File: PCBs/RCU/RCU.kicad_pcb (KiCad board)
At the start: 4 copper layers, 99 x 139 mm, 148 parts, among them J100 Conn_01x02, J200 USB_C_Receptacle_USB2.0, J201 Conn_01x05, J300 Right_Motor_Screw_Terminal, J301 Right_Encoder_Conn, J302 Left_Motor_Screw_Terminal, J303 Left_Encoder_Conn, J400 USB_C_Receptacle_USB2.0, Q400 2N7002NXAKR (NMOS), Q401 2N7002NXAKR (NMOS), Q402 BSS84AK,215 (PMOS), Q403 2N7002NXAKR (NMOS), SW201 SW_Push, SW400 SW_Push, SW401 SW_SPDT, U100 LM2576S-ADJ, U101 AP63203WU, U102 AZ1117-3.3, U200 STM32G0B1CBT6, U201 USBLC6-2SC6, U300 OPA320, U301 DRV8876, U302 OPA320, U303 DRV8876, U400 USBLC6-2SC6, U401 CH340C, U402 ESP32-MINI-1, U403 DG2788ADN-T1-GE4, U500 APDS-9306-065, U501 LSM6DS3, U502 SHT30-DIS, U600 ADC121C027CIMK/NOPB, U601 OPA320, U602 ADC121C027CIMK/NOPB, U603 OPA320, U700 SST26VF032BT-104I/SM, Y200 16MHz

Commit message: Course layout complete, added all 3d models
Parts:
- moved D104 35.0 mm to (128.5, 28.1)
- moved D103 23.2 mm to (130.1, 32.7), turned to -90 degrees
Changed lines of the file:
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@@
     (pad "2" smd rect (at 1.59 0 270) (size 1.18 1.17) (layers "F.Cu" "F.Paste" "F.Mask")
       (net 8 "+5C") (pinfunction "A") (pintype "passive") (solder_mask_margin 0.102))
+    (model "${KICAD6_3DMODEL_DIR}/Diode_SMD.3dshapes/D_SOD-123F.step"
+      (offset (xyz 0 0 0))
+      (scale (xyz 1 1 1))
+      (rotate (xyz 0 0 0))
+    )
   )
   (footprint "Resistor_SMD:R_0603_1608Metric" (layer "F.Cu")
@@
     (pad "2" smd rect (at 1.59 0) (size 1.18 1.17) (layers "F.Cu" "F.Paste" "F.Mask")
       (net 1 "+BATT") (pinfunction "A") (pintype "passive") (solder_mask_margin 0.102))
+    (model "${KICAD6_3DMODEL_DIR}/Diode_SMD.3dshapes/D_SOD-123F.step"
+      (offset (xyz 0 0 0))
+      (scale (xyz 1 1 1))
+      (rotate (xyz 0 0 0))
+    )
   )
   (footprint "Resistor_SMD:R_0603_1608Metric" (layer "F.Cu")
@@
   )
   (footprint "Schottky_Diode:SODFL3719X135N" (layer "F.Cu")
-    (at 152.5 26.7)
+    (at 130.1 32.7 -90)
     (property "Sheetfile" "Power.kicad_sch")
     (property "Sheetname" "[1] Power")
     (attr smd)
-    (fp_text reference "D103" (at 0.07 -2.2) (layer "F.SilkS")
+    (fp_text reference "D103" (at 0.07 -2.2 90) (layer "F.SilkS")
       (effects (font (size 0.787402 0.787402) (thickness 0.15)))
     )
-    (fp_text value "SM5817" (at 4.57 2.2) (layer "F.Fab")
+    (fp_text value "SM5817" (at 4.57 2.2 90) (layer "F.Fab")
       (effects (font (size 0.787402 0.787402) (thickness 0.15)))
     )
@@
     (fp_line (start -1.425 -0.95) (end -1.425 0.95) (layer "F.Fab") (width 0.127))
     (fp_circle (center -3.18 0) (end -3.08 0) (layer "F.Fab") (width 0.2) (fill none))
-    (pad "1" smd rect (at -1.59 0) (size 1.18 1.17) (layers "F.Cu" "F.Paste" "F.Mask")
+    (pad "1" smd rect (at -1.59 0 270) (size 1.18 1.17) (layers "F.Cu" "F.Paste" "F.Mask")
       (net 29 "Net-(D103-Pad1)") (pinfunction "K") (pintype "passive") (solder_mask_margin 0.102))
-    (pad "2" smd rect (at 1.59 0) (size 1.18 1.17) (layers "F.Cu" "F.Paste" "F.Mask")
+    (pad "2" smd rect (at 1.59 0 270) (size 1.18 1.17) (layers "F.Cu" "F.Paste" "F.Mask")
       (net 12 "+5F") (pinfunction "A") (pintype "passive") (solder_mask_margin 0.102))
+    (model "${KICAD6_3DMODEL_DIR}/Diode_SMD.3dshapes/D_SOD-123F.step"
+      (offset (xyz 0 0 0))
+      (scale (xyz 1 1 1))
+      (rotate (xyz 0 0 0))
+    )
   )
   (footprint "Capacitor_SMD:C_0603_1608Metric" (layer "F.Cu")
@@
   )
   (footprint "Schottky_Diode:SODFL3719X135N" (layer "F.Cu")
-    (at 163.5 26.7)
+    (at 128.5 28.1)
     (property "Sheetfile" "Power.kicad_sch")
     (property "Sheetname" "[1] Power")
@@
     (pad "2" smd rect (at 1.59 0) (size 1.18 1.17) (layers "F.Cu" "F.Paste" "F.Mask")
       (net 29 "Net-(D103-Pad1)") (pinfunction "A") (pintype "passive") (solder_mask_margin 0.102))
+    (model "${KICAD6_3DMODEL_DIR}/Diode_SMD.3dshapes/D_SOD-123F.step"
+      (offset (xyz 0 0 0))
+      (scale (xyz 1 1 1))
+      (rotate (xyz 0 0 0))
+    )
   )
   (footprint "Resistor_SMD:R_0603_1608Metric" (layer "F.Cu")

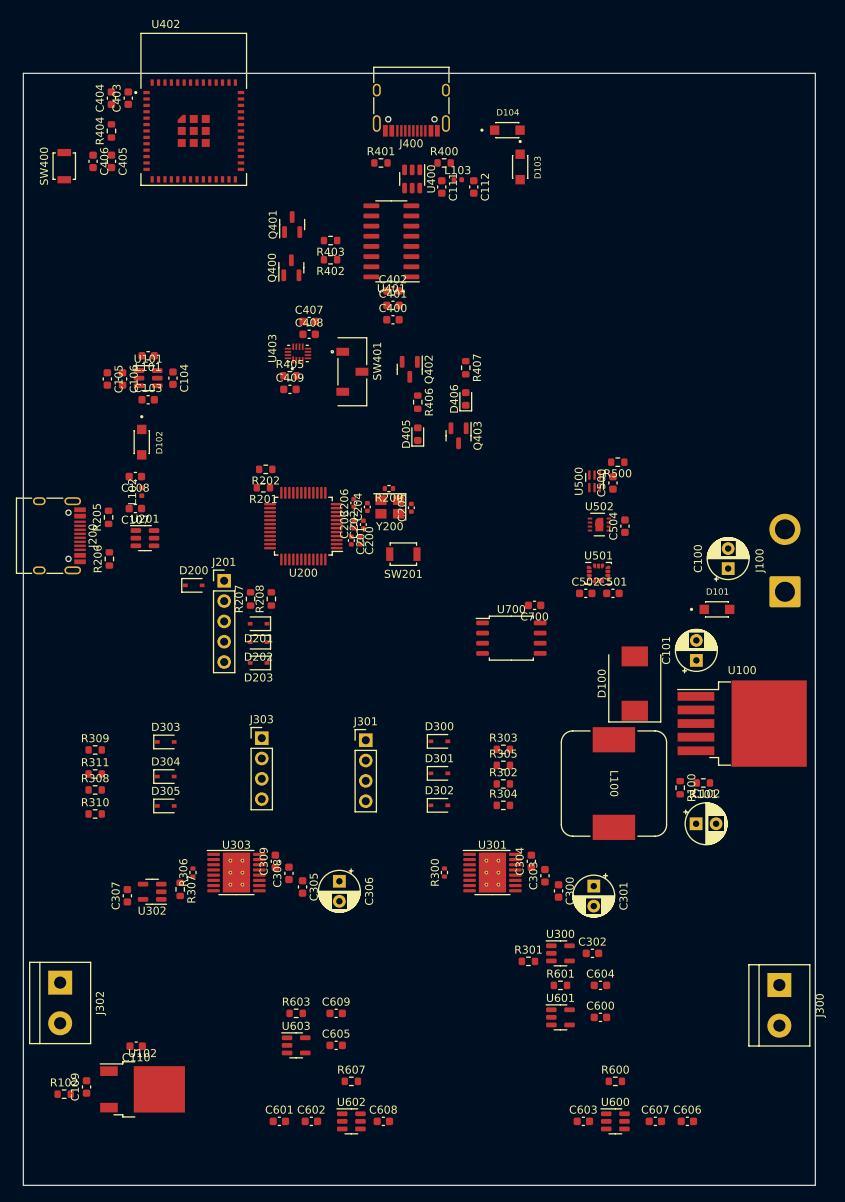
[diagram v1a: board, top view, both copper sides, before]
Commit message: Added drill/place file and grid origin
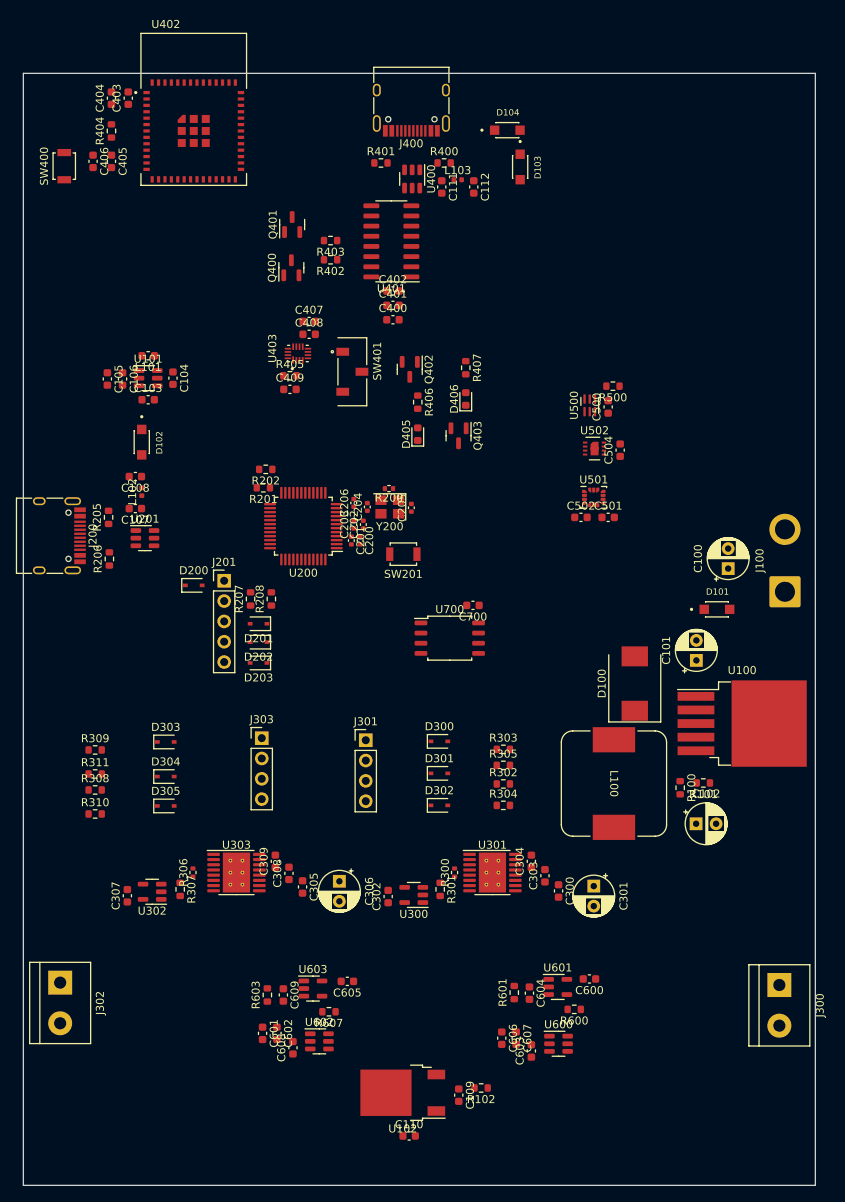
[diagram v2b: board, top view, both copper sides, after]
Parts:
- moved R102 52.1 mm to (125.2, 147.8), turned to 180 degrees
- moved C109 46.5 mm to (122.4, 148.7), turned to -90 degrees
- moved C110 35.9 mm to (116.2, 153.8), turned to 0 degrees
- moved U102 32.5 mm to (115.4, 148.4), turned to 180 degrees
- moved C302 26.5 mm to (113.6, 123.9), turned to 90 degrees
- moved C606 25.4 mm to (127.8, 141.6), turned to -90 degrees
- moved C607 20.3 mm to (129.6, 141.6), turned to -90 degrees
- moved U300 19.7 mm to (116.8, 123.7), turned to 180 degrees
- moved C608 14.6 mm to (101.7, 142.8), turned to 90 degrees
- moved R301 14.2 mm to (120.1, 123.0), turned to -90 degrees
- moved U600 12.0 mm to (134.9, 142.3)
- moved C602 11.8 mm to (99.7, 141.0), turned to -90 degrees
- moved C601 11.2 mm to (97.9, 141.0), turned to -90 degrees
- moved C603 10.9 mm to (131.5, 143.2), turned to 90 degrees
- moved U602 10.8 mm to (105.0, 142.0)
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
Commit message: More rearangment, added 3d model to light and temp/humidity sensor
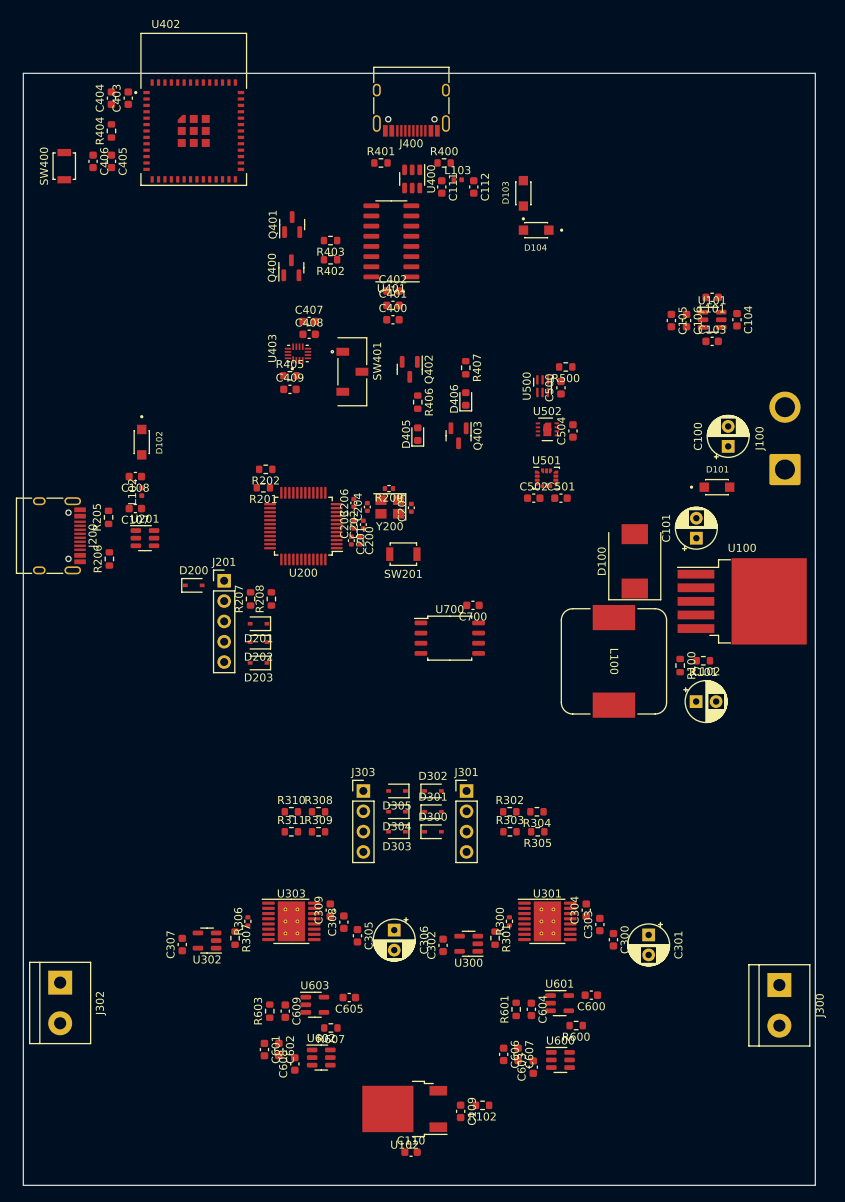
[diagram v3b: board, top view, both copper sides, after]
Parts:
- moved C103 70.9 mm to (154.1, 54.5)
- moved C104 70.9 mm to (157.2, 51.8)
- moved C105 70.9 mm to (149.0, 51.9)
- moved C106 70.9 mm to (150.9, 51.9)
- moved L101 70.9 mm to (154.1, 49.0)
- moved U101 70.9 mm to (154.1, 51.8)
- moved D303 31.0 mm to (114.7, 115.8), turned to 180 degrees
- moved R309 29.7 mm to (104.9, 115.8)
- moved D304 29.2 mm to (114.7, 113.3), turned to 180 degrees
- moved D305 29.0 mm to (114.7, 110.7), turned to 180 degrees
- moved R308 28.1 mm to (104.9, 113.3)
- moved R311 25.6 mm to (101.5, 115.8)
- moved R310 24.5 mm to (101.5, 113.3)
- moved C100 15.3 mm to (156.1, 67.6)
- moved D100 15.3 mm to (144.4, 82.0)
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
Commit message: Performed ground pour on internal ground layer
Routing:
- net +3V3: track 0.00 -> 6.09 mm
- added copper zone on F.Cu, net GND
- added copper zone on In1.Cu, net GND
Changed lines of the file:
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@@
   (gr_line (start 68 160) (end 68 21) (layer "Edge.Cuts") (width 0.1))
   (gr_line (start 167 160) (end 68 160) (layer "Edge.Cuts") (width 0.1))
+  (segment (start 108.43 78.35) (end 109 78.92) (width 0.3) (layer "F.Cu") (net 6))
+  (segment (start 109 78.92) (end 108.93 78.85) (width 0.3) (layer "F.Cu") (net 6))
+  (segment (start 109.27 77.85) (end 109.3 77.88) (width 0.3) (layer "F.Cu") (net 6))
+  (segment (start 107.1625 77.85) (end 109.27 77.85) (width 0.3) (layer "F.Cu") (net 6))
+  (segment (start 108.93 78.85) (end 107.1625 78.85) (width 0.3) (layer "F.Cu") (net 6))
+  (segment (start 107.1625 78.35) (end 108.43 78.35) (width 0.3) (layer "F.Cu") (net 6))
+  (zone (net 2) (net_name "GND") (layer "F.Cu") (hatch edge 0.508)
+    (connect_pads yes (clearance 0.15))
+    (min_thickness 0.254) (filled_areas_thickness no)
+    (fill yes (thermal_gap 0.508) (thermal_bridge_width 0.508))
+    (polygon
+      (pts
+        (xy 110.6 80.4)
+        (xy 108.5 80.4)
+        (xy 108.5 79.5)
+        (xy 110.6 79.5)
+      )
+    )
+  )
+  (zone (net 2) (net_name "GND") (layer "In1.Cu") (hatch edge 0.508)
+    (connect_pads (clearance 0.4))
+    (min_thickness 0.3) (filled_areas_thickness no)
+    (fill yes (thermal_gap 0.508) (thermal_bridge_width 0.508))
+    (polygon
+      (pts
+        (xy 167 160)
+        (xy 68 160)
+        (xy 68 21)
+        (xy 167 21)
+      )
+    )
+  )
 )

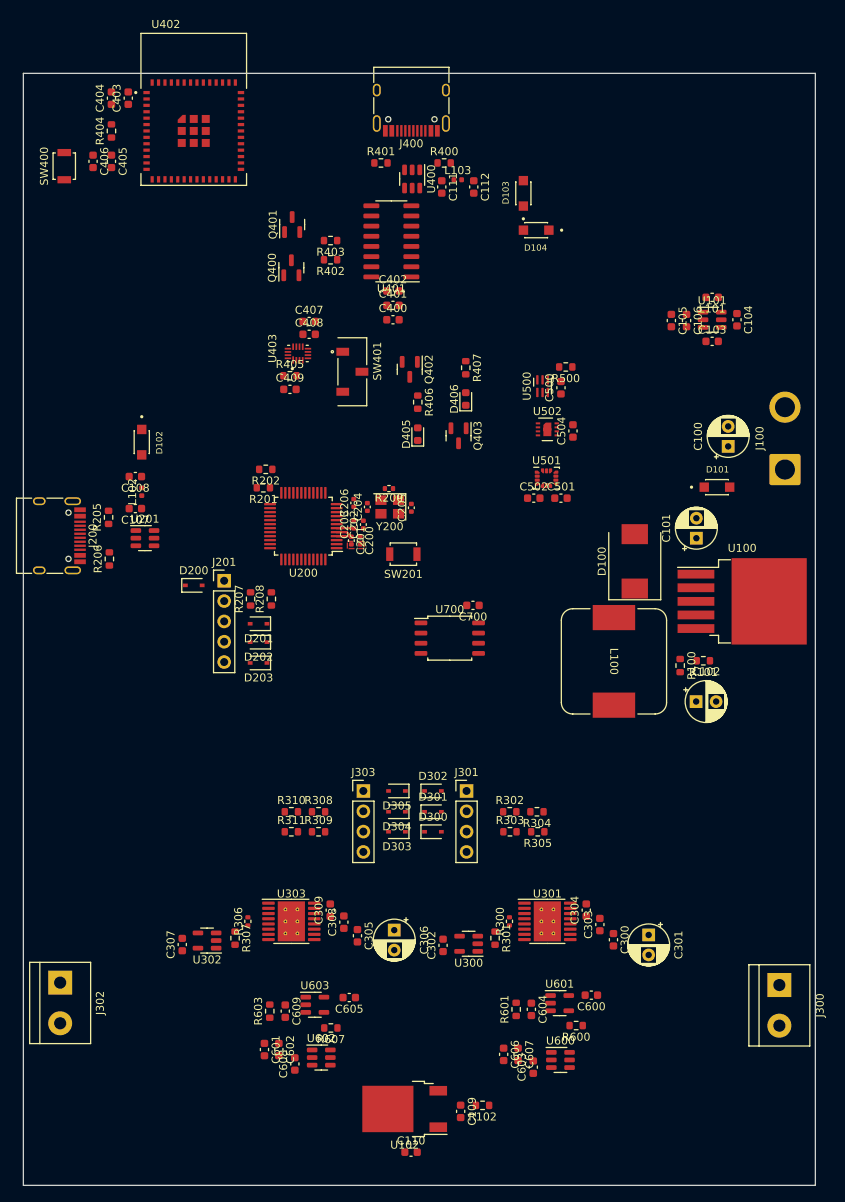
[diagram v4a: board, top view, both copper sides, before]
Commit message: Made text designators invisible
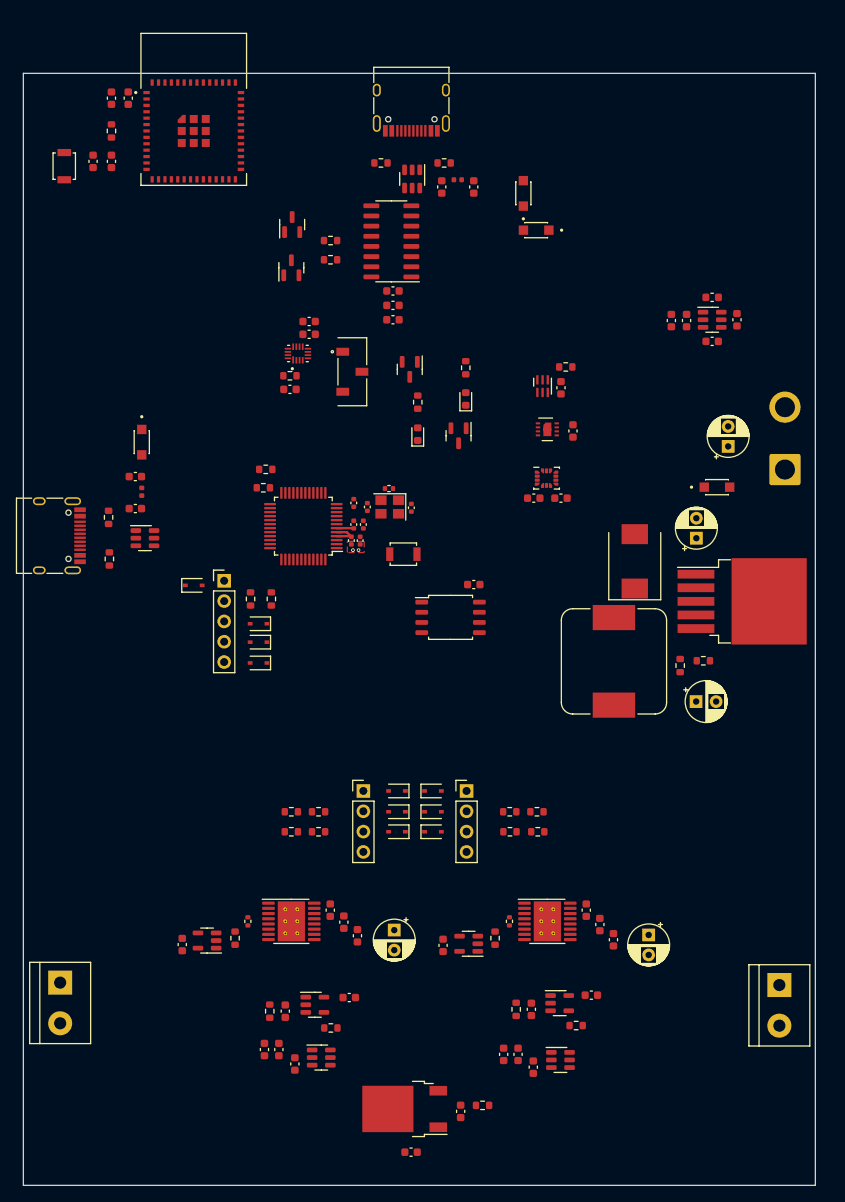
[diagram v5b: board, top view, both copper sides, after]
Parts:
- moved U700 2.60 mm to (121.4, 89.0)
- moved C700 2.60 mm to (124.3, 84.9)
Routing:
- net GND: vias 0 -> 2

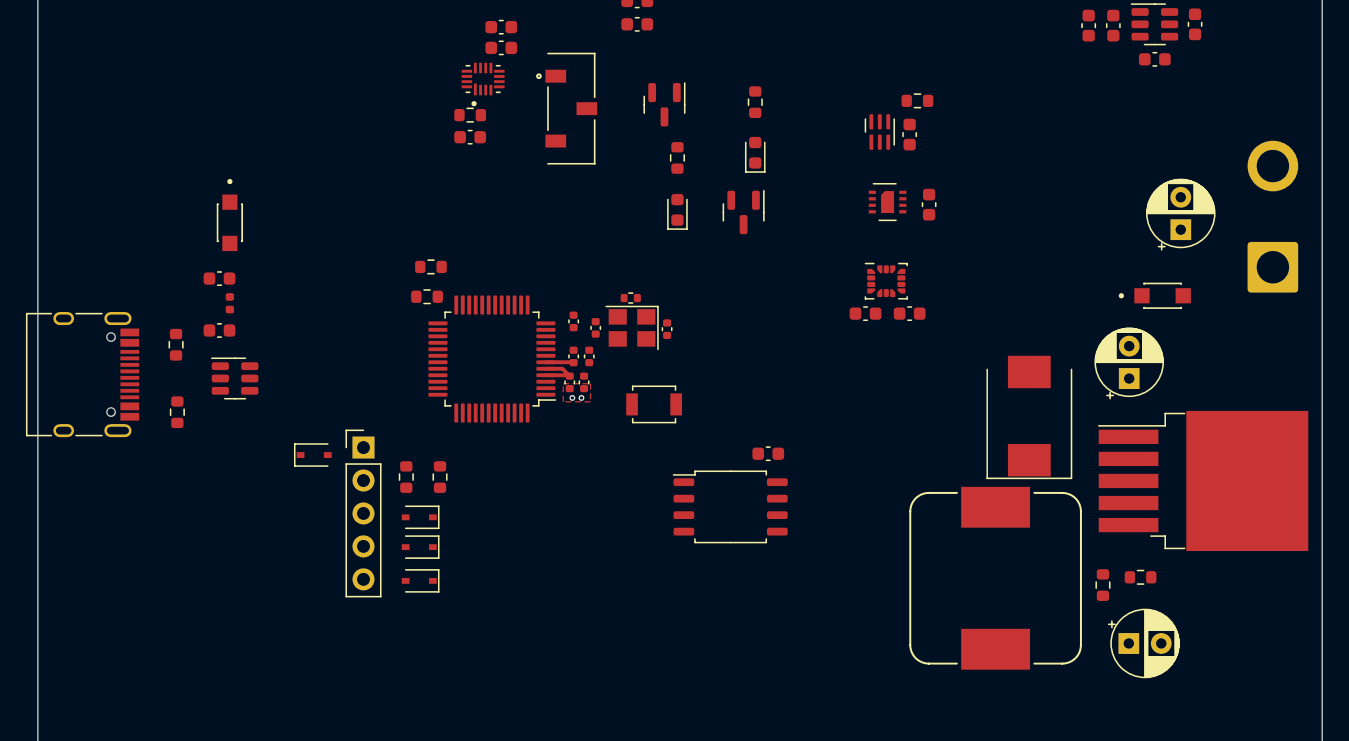
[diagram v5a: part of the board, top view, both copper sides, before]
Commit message: Added split 3.3V and 6V VCC plane
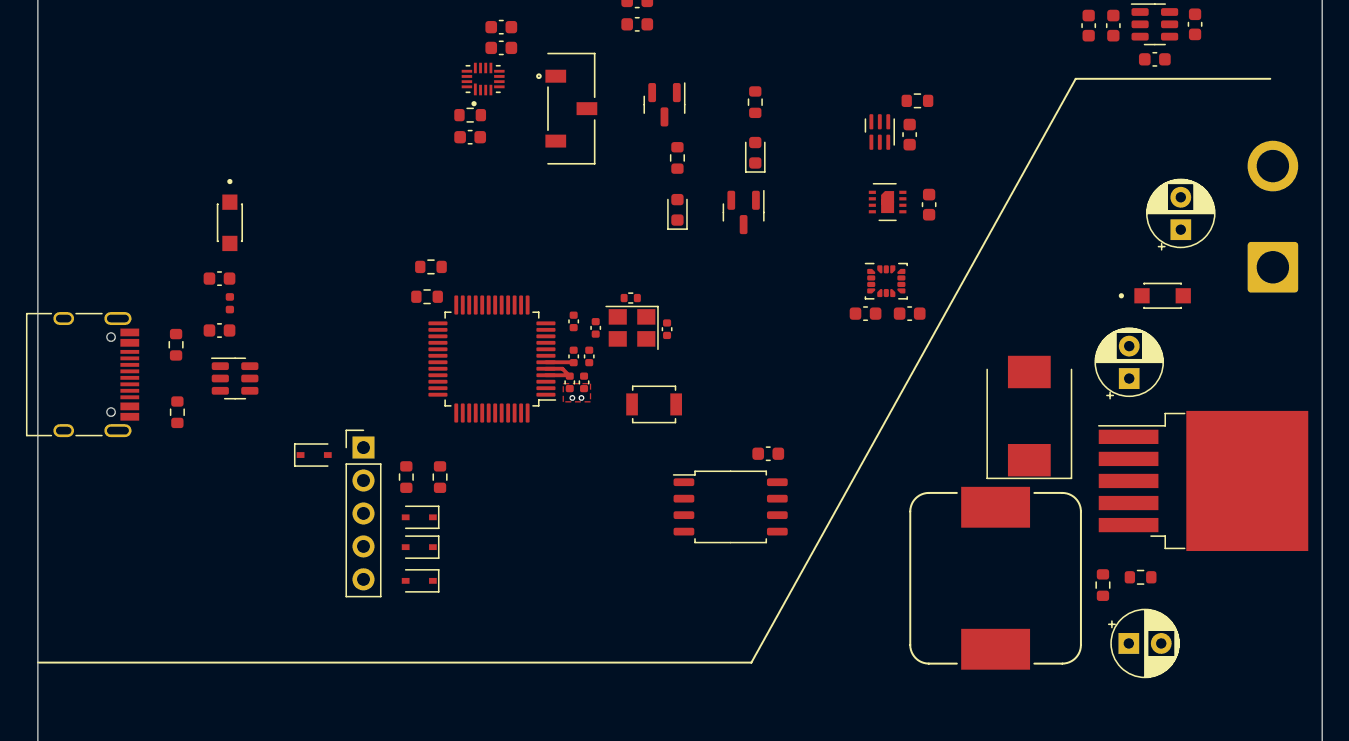
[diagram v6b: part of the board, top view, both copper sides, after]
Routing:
- added copper zone on In2.Cu, net +3V3
- added copper zone on In2.Cu, net +6V
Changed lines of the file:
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@@
     )
   )
+  (gr_line (start 68 101) (end 123 101) (layer "F.SilkS") (width 0.15))
+  (gr_line (start 148 56) (end 163 56) (layer "F.SilkS") (width 0.15))
+  (gr_line (start 123 101) (end 148 56) (layer "F.SilkS") (width 0.15))
   (gr_line (start 167 21) (end 167 160) (layer "Edge.Cuts") (width 0.1))
   (gr_line (start 68 21) (end 167 21) (layer "Edge.Cuts") (width 0.1))
@@
       )
     )
+  )
+  (zone (net 6) (net_name "+3V3") (layer "In2.Cu") (hatch edge 0.508)
+    (connect_pads (clearance 0.4))
+    (min_thickness 0.3) (filled_areas_thickness no)
+    (fill yes (thermal_gap 0.508) (thermal_bridge_width 0.508))
+    (polygon
+      (pts
+        (xy 167 56)
+        (xy 148 56)
+        (xy 123 101)
+        (xy 68 101)
+        (xy 68 21)
+        (xy 167 21)
+      )
+    )
+  )
+  (zone (net 13) (net_name "+6V") (layer "In2.Cu") (hatch edge 0.508)
+    (connect_pads (clearance 0.4))
+    (min_thickness 0.3) (filled_areas_thickness no)
+    (fill yes (thermal_gap 0.508) (thermal_bridge_width 0.508))
+    (polygon
+      (pts
+        (xy 167 160)
+        (xy 68 160)
+        (xy 68 102)
+        (xy 124 102)
+        (xy 148 57)
+        (xy 167 57)
+      )
+    )
